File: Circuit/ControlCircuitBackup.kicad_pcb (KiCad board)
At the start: 2 copper layers, 79 parts, among them CON501 AVR-ISP-10, IC501 ATMEGA644-A, K201 Meisei-m4-24h, K202 Meisei-m4-24h, K203 Meisei-m4-24h, K204 Meisei-m4-24h, K205 Meisei-m4-24h, K206 Meisei-m4-24h, K207 Meisei-m4-24h, K208 Meisei-m4-24h, P101 CONN_01X08, P102 CONN_01X08, P103 CONN_01X08, P104 CONN_01X08, P105 CONN_01X08, P106 CONN_01X08, P107 CONN_01X02, Q201 Q_NPN_BCE, Q202 Q_NPN_BCE, Q203 Q_NPN_BCE, Q204 Q_NPN_BCE, Q205 Q_NPN_BCE, Q206 Q_NPN_BCE, Q207 Q_NPN_BCE, Q208 Q_NPN_BCE, U301 LTV-817, U302 LTV-817, U303 LTV-817, U304 LTV-817, U305 LTV-817, U306 LTV-817, U307 LTV-817, U308 LTV-817, Y501 Crystal

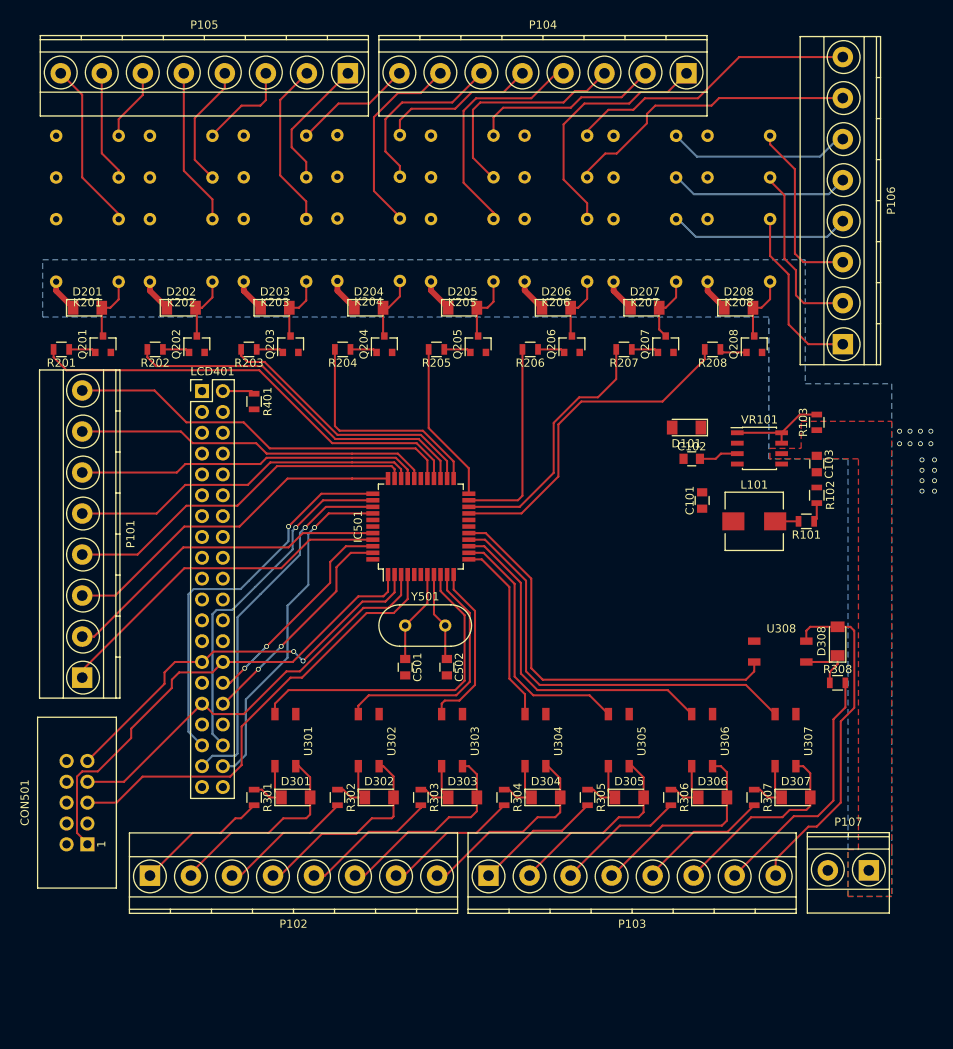
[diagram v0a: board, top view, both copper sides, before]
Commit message: Routed PCB and made backup. Footprint for Optocouplers
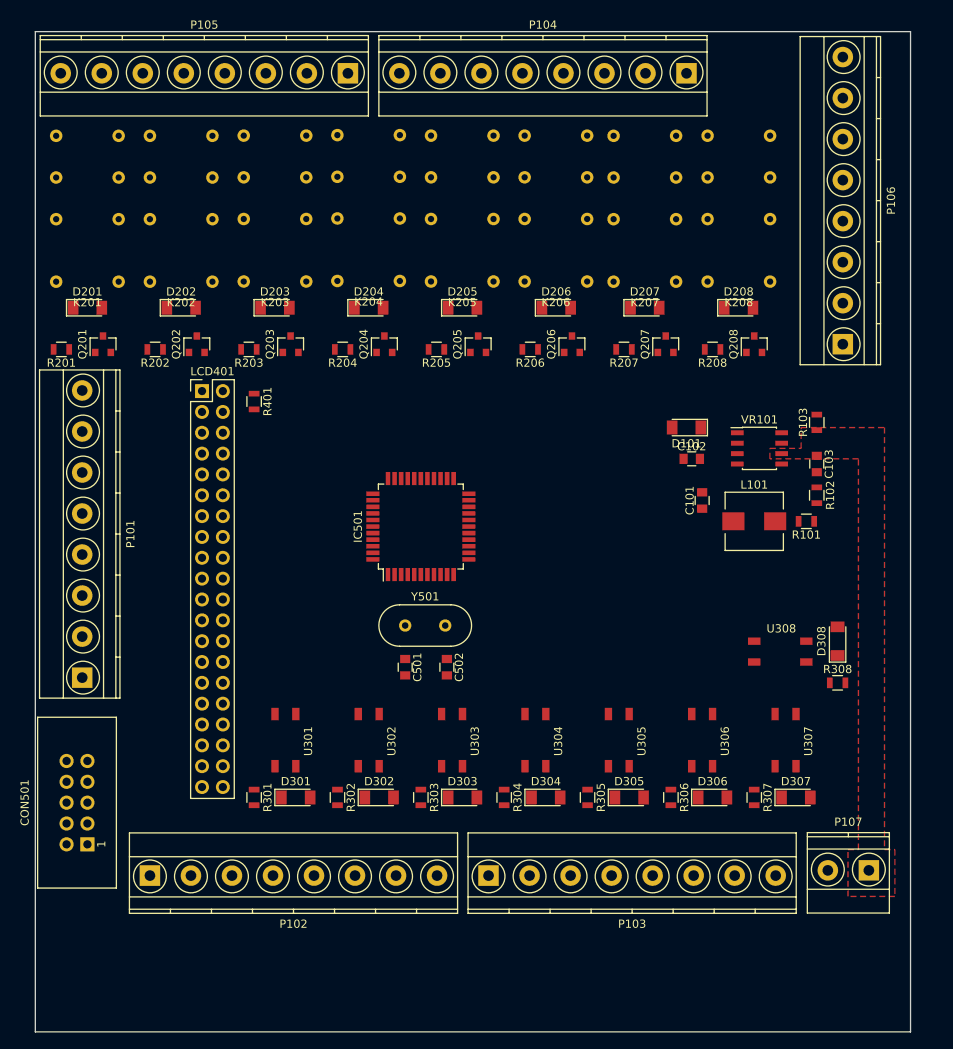
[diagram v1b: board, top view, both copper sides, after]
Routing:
- net /LCDTouchScreen/MOSI: track 59.4 -> 0.00 mm
- net /Microcontroller/RESET: track 55.1 -> 0.00 mm
- net /RelayOutputs/O1: track 54.7 -> 0.00 mm
- net /RelayInputs/I7: track 52.6 -> 0.00 mm
- net /LCDTouchScreen/SCK: track 51.2 -> 0.00 mm
- net /RelayInputs/I8: track 50.2 -> 0.00 mm
- net /LCDTouchScreen/MISO: track 50.0 -> 0.00 mm, vias 2 -> 0
- net /AVCC: track 47.8 -> 0.00 mm
- net /Microcontroller/ADC0: track 47.8 -> 0.00 mm, vias 1 -> 0
- net /Microcontroller/ADC2: track 45.2 -> 0.00 mm, vias 1 -> 0
- net /RelayOutputs/O2: track 44.1 -> 0.00 mm
- net /Microcontroller/ADC5: track 43.8 -> 0.00 mm
- net /AREF: track 43.5 -> 0.00 mm
- net /Microcontroller/ADC4: track 43.2 -> 0.00 mm
- net /Microcontroller/ADC1: track 43.2 -> 0.00 mm, vias 1 -> 0
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- removed copper zone on B.Cu, net +24V
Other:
- board outline added: 106.7 x 121.9 mm
- net class Power removed
